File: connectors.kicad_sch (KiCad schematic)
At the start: 0 parts

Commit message: [#51627] Deserializer: add connections and passives
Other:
- company: (none) -> Antmicro Ltd
- title: (none) -> GMSL Deserializer
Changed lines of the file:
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@@
 (kicad_sch (version 20211123) (generator eeschema)
   (paper "A3")
+  (title_block
+    (title "GMSL Deserializer")
+    (date "2023-11-23")
+    (rev "1.0.0")
+    (company "Antmicro Ltd")
+    (comment 1 "www.antmicro.com")
+  )
 )

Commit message: [#51628] Connectors: add CSI mux and FFC connectors
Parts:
- added C? (x4): C_1u_0402, jetson-orin-baseboard-footprints:C_0402_1005Metric, symbol jetson-orin-baseboard:C_1u_0402
- added D? (x4): LED_G_0603_LTST-C190GKT, jetson-orin-baseboard-footprints:LED_0603_1608Metric_G, symbol jetson-orin-baseboard:LED_G_0603_LTST-C190GKT
- added J? (x2): Conn_FFC_68715014522_ONE-SIDE, jetson-orin-baseboard-footprints:WE_68715014522_ONE-SIDE, symbol jetson-orin-baseboard:Conn_FFC_68715014522_ONE-SIDE
- added R? (x6): R_4x0R_0201_array, jetson-orin-baseboard-footprints:R_Array_4x0201_Panasonic_EXB18V, symbol jetson-orin-baseboard:R_4x0R_0201_array
- added R? (x2): R_470R_0402, jetson-orin-baseboard-footprints:R_0402_1005Metric, symbol jetson-orin-baseboard:R_470R_0402
- added R? (x2): R_200R_0402, jetson-orin-baseboard-footprints:R_0402_1005Metric, symbol jetson-orin-baseboard:R_200R_0402
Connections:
- new net: D?.1, R?.1 (x4)
- new net: J?.42, R?.5 (R4.2) (x2)
- new net: J?.41, R?.6 (R3.2) (x2)
- new net: J?.40, R?.7 (R2.2) (x2)
- new net: J?.39, R?.8 (R1.2) (x2)
- new net CSI0_CLK_N: J?.10
- new net CSI0_CLK_P: J?.11
- new net CSI0_D0_N: J?.7, R?.3 (R3.1), R?.3 (R3.1)
- new net CSI0_D0_P: J?.8, R?.4 (R4.1), R?.4 (R4.1)
- new net CSI0_D1_N: R?.1 (R1.1), R?.1 (R1.1)
- new net CSI0_D1_P: J?.6, R?.2 (R2.1), R?.2 (R2.1)
- new net CSI1_0_D0_N: J?.3
- new net CSI1_0_D0_P: J?.4
- new net CSI1_0_D1_N: J?.1
- new net CSI1_0_D1_P: J?.2
- new net CSI1_1_D0_N: J?.7
- new net CSI1_1_D0_P: J?.8
- new net CSI1_1_D1_N: J?.5
- new net CSI1_1_D1_P: J?.6
- new net CSI1_CLK_N: J?.10
- new net CSI1_CLK_P: J?.11
- new net CSI2_CLK_N: J?.28
- new net CSI2_CLK_P: J?.29
- new net CSI2_D0_N: J?.25, R?.3 (R3.1), R?.3 (R3.1)
- new net CSI2_D0_P: J?.26, R?.4 (R4.1), R?.4 (R4.1)
- new net CSI2_D1_N: J?.23, R?.1 (R1.1), R?.1 (R1.1)
- new net CSI2_D1_P: J?.24, R?.2 (R2.1), R?.2 (R2.1)
- new net CSI3_0_D0_N: J?.21
- new net CSI3_0_D0_P: J?.22
- new net CSI3_0_D1_N: J?.19
- new net CSI3_0_D1_P: J?.20
- new net CSI3_1_D0_N: J?.25
- new net CSI3_1_D0_P: J?.26
- new net CSI3_1_D1_N: J?.23
- new net CSI3_1_D1_P: J?.24
- new net CSI3_CLK_N: J?.28
- new net CSI3_CLK_P: J?.29
- new net CSIA_3V3: C?.2, J?.47, J?.48, R?.2
- new net CSIA_5V: C?.2, J?.49, J?.50, R?.2
- new net CSIB_3V3: C?.2, J?.47, J?.48, R?.2
- new net CSIB_5V: C?.2, J?.49, J?.50, R?.2
- new net GND: C?.1, C?.1, C?.1, C?.1, D?.2, D?.2, D?.2, D?.2, J?.12, J?.12, J?.15, J?.15, J?.18, J?.18, J?.27, J?.27, J?.30, J?.30, J?.9, J?.9, J?.SH, J?.SH
- new net SCL_CAM0: R?.2 (R2.1)
- new net SCL_CAM1: R?.4 (R4.1)
- new net SCL_CAM2: R?.2 (R2.1)
- new net SCL_CAM3: R?.4 (R4.1)
- new net SDA_CAM0: R?.1 (R1.1)
- new net SDA_CAM1: R?.3 (R3.1)
- new net SDA_CAM2: R?.1 (R1.1)
- new net SDA_CAM3: R?.3 (R3.1)
- new net VSYNC_CAM0_3V3: J?.32
- new net VSYNC_CAM1_3V3: J?.34
- new net VSYNC_CAM2_3V3: J?.32
- new net VSYNC_CAM3_3V3: J?.34
- no-connect marks 0 -> 36
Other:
- note added: "CSI Mux"
- note added: "CSI connector J?"
- note added: "CSI0 x2"
- note added: "CSI0 x4"
- note added: "CSI1 x2"
- note added: "CSI2 x2"
- note added: "CSI2 x4"
- note added: "CSI3 x2"

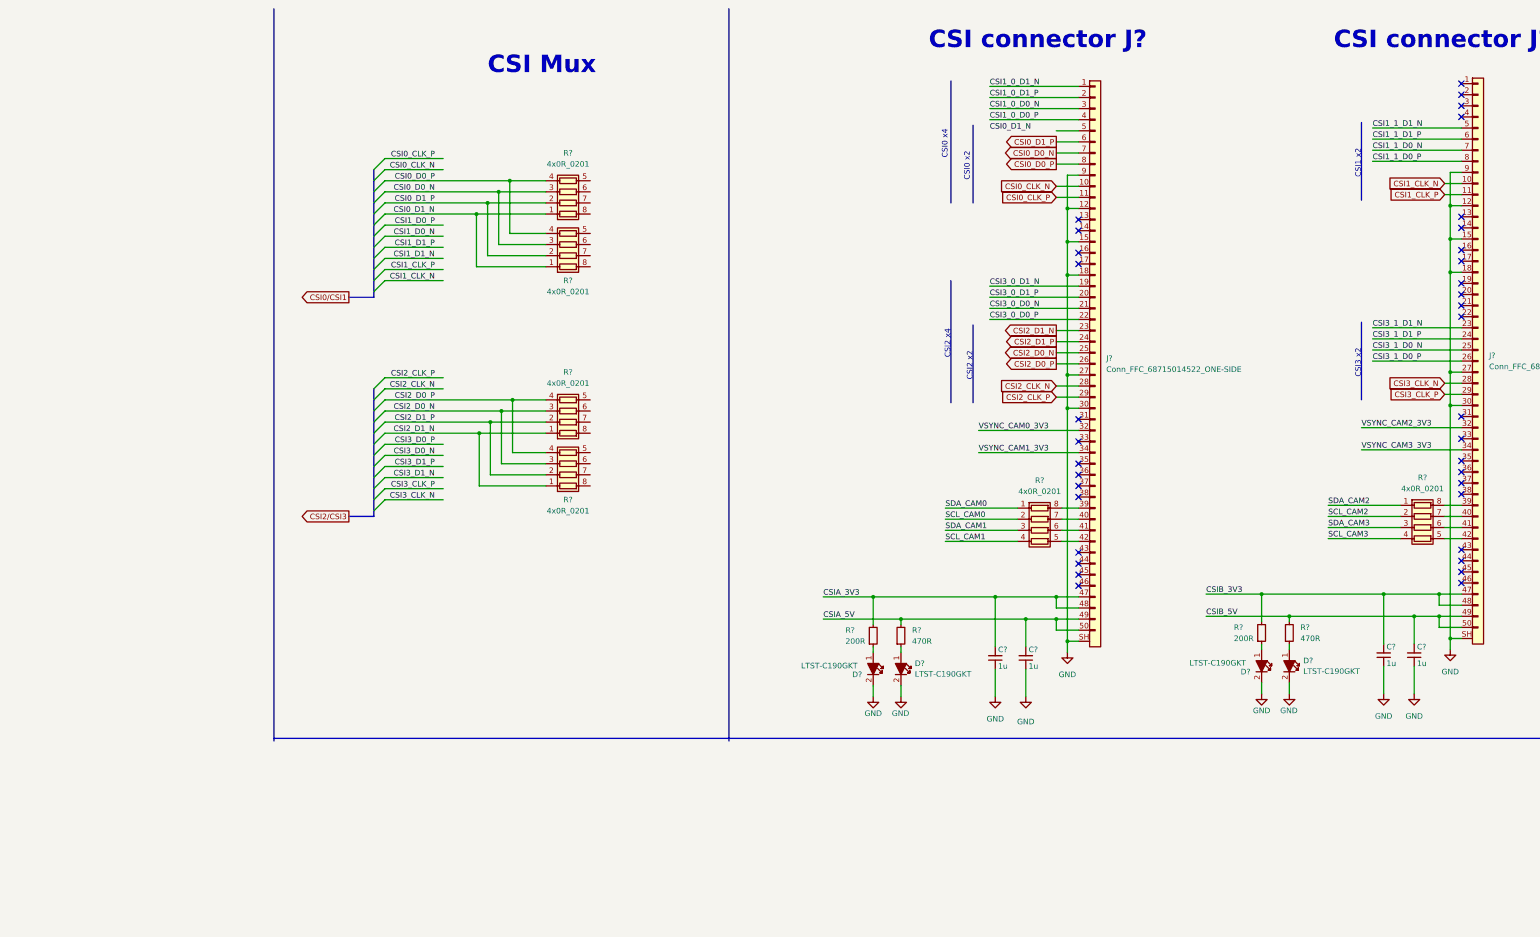
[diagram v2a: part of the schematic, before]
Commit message: [#51628] Connectors: add FAKRA connectors and CSI nets
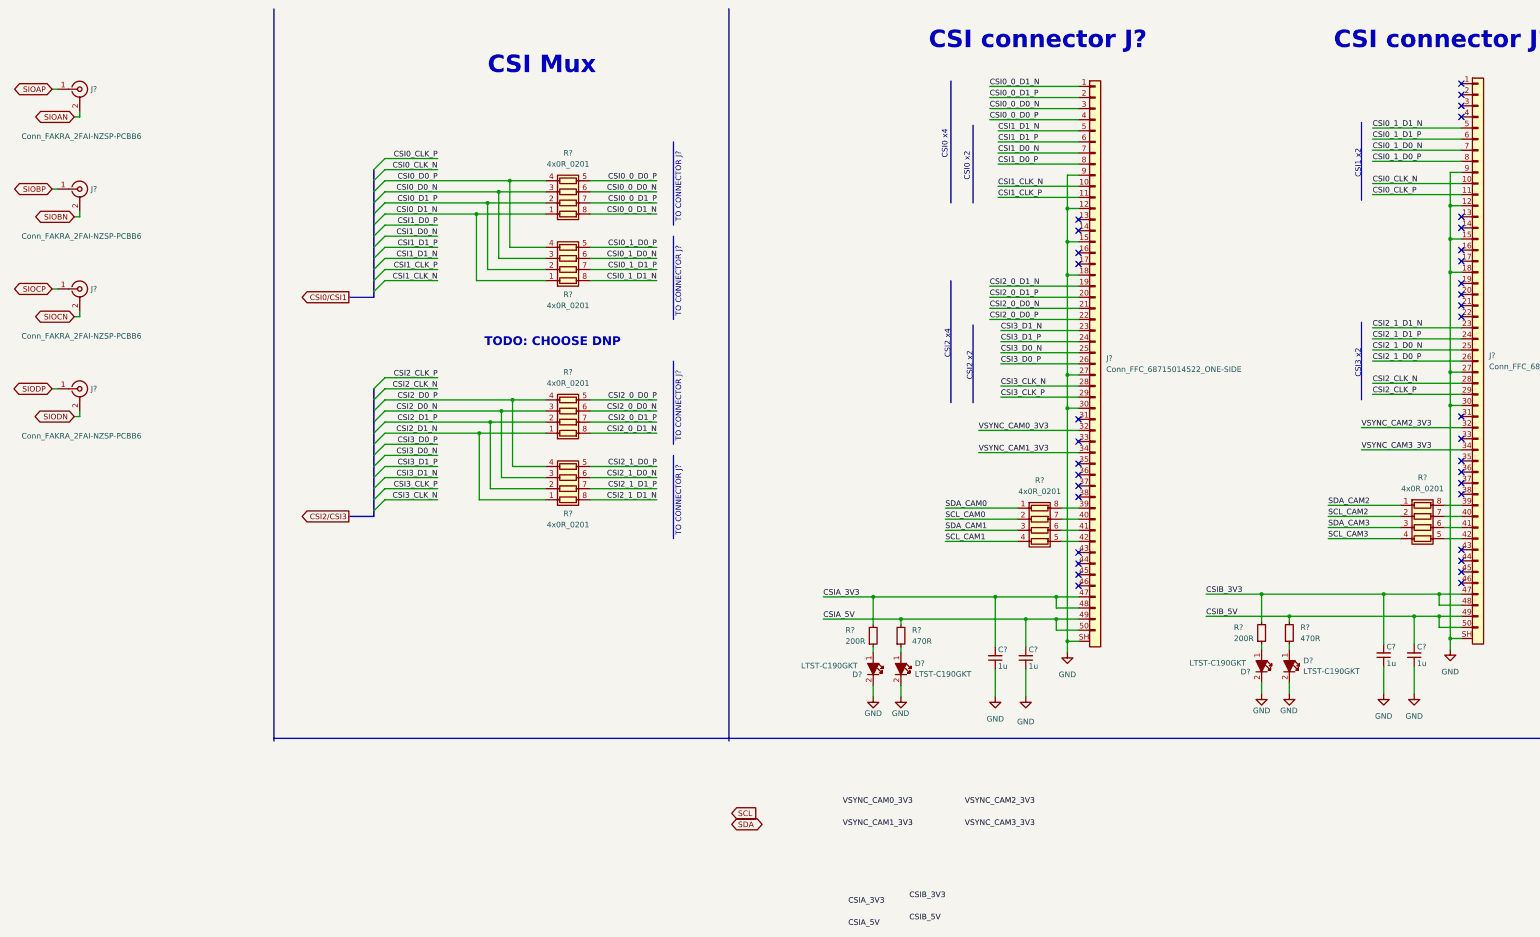
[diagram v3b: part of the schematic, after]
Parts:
- added J? (x4): Conn_FAKRA_2FAI-NZSP-PCBB6, antmicro-footprints:Conn_FAKRA_2FAI-NXSP-PCBB6, symbol antmicroCoaxialConnectorsRF:Conn_FAKRA_2FAI-NZSP-PCBB6
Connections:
- net CSI1_0_D0_N is gone; now on net CSI0_0_D0_N: J?.3
- net CSI1_0_D0_P is gone; now on net CSI0_0_D0_P: J?.4
- net CSI1_0_D1_N is gone; now on net CSI0_0_D1_N: J?.1
- net CSI1_0_D1_P is gone; now on net CSI0_0_D1_P: J?.2
- net CSI1_1_D0_N is gone; now on net CSI0_1_D0_N: J?.7
- net CSI1_1_D0_P is gone; now on net CSI0_1_D0_P: J?.8
- net CSI1_1_D1_N is gone; now on net CSI0_1_D1_N: J?.5
- net CSI1_1_D1_P is gone; now on net CSI0_1_D1_P: J?.6
- net CSI3_0_D0_N is gone; now on net CSI2_0_D0_N: J?.21
- net CSI3_0_D0_P is gone; now on net CSI2_0_D0_P: J?.22
- net CSI3_0_D1_N is gone; now on net CSI2_0_D1_N: J?.19
- net CSI3_0_D1_P is gone; now on net CSI2_0_D1_P: J?.20
- net CSI3_1_D0_N is gone; now on net CSI2_1_D0_N: J?.25
- net CSI3_1_D0_P is gone; now on net CSI2_1_D0_P: J?.26
- net CSI3_1_D1_N is gone; now on net CSI2_1_D1_N: J?.23
- net CSI3_1_D1_P is gone; now on net CSI2_1_D1_P: J?.24
- net CSI0_CLK_N: now also J?.10; no longer J?.10
- net CSI0_CLK_P: now also J?.11; no longer J?.11
- net CSI0_D0_N: no longer J?.7
- net CSI0_D0_P: no longer J?.8
- net CSI0_D1_P: no longer J?.6
- net CSI1_CLK_N: now also J?.10; no longer J?.10
- net CSI1_CLK_P: now also J?.11; no longer J?.11
- net CSI1_D0_N: now also J?.7
- net CSI1_D0_P: now also J?.8
- net CSI1_D1_N: now also J?.5
- net CSI1_D1_P: now also J?.6
- net CSI2_CLK_N: now also J?.28; no longer J?.28
- net CSI2_CLK_P: now also J?.29; no longer J?.29
- net CSI2_D0_N: no longer J?.25
- net CSI2_D0_P: no longer J?.26
- net CSI2_D1_N: no longer J?.23
- net CSI2_D1_P: no longer J?.24
- net CSI3_CLK_N: now also J?.28; no longer J?.28
- net CSI3_CLK_P: now also J?.29; no longer J?.29
- net CSI3_D0_N: now also J?.25
- net CSI3_D0_P: now also J?.26
- net CSI3_D1_N: now also J?.23
- net CSI3_D1_P: now also J?.24
- net CSI0_0_D0_P: now reaches R?.5 (R4.2)
- net CSI0_0_D0_N: now reaches R?.6 (R3.2)
- net CSI0_0_D1_P: now reaches R?.7 (R2.2)
- net CSI0_0_D1_N: now reaches R?.8 (R1.2)
- net CSI0_1_D0_P: now reaches R?.5 (R4.2)
- net CSI0_1_D0_N: now reaches R?.6 (R3.2)
- net CSI0_1_D1_P: now reaches R?.7 (R2.2)
- net CSI0_1_D1_N: now reaches R?.8 (R1.2)
- net CSI2_1_D0_P: now reaches R?.5 (R4.2)
- net CSI2_1_D0_N: now reaches R?.6 (R3.2)
- net CSI2_1_D1_P: now reaches R?.7 (R2.2)
- net CSI2_1_D1_N: now reaches R?.8 (R1.2)
- net CSI2_0_D0_P: now reaches R?.5 (R4.2)
- net CSI2_0_D0_N: now reaches R?.6 (R3.2)
- net CSI2_0_D1_P: now reaches R?.7 (R2.2)
- net CSI2_0_D1_N: now reaches R?.8 (R1.2)
- new net SIOAN: J?.2, J?.3, J?.4, J?.5
- new net SIOAP: J?.1
- new net SIOBN: J?.2, J?.3, J?.4, J?.5
- new net SIOBP: J?.1
- new net SIOCN: J?.2, J?.3, J?.4, J?.5
- new net SIOCP: J?.1
- new net SIODN: J?.2, J?.3, J?.4, J?.5
- new net SIODP: J?.1
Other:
- note added: "TO CONNECTOR J?"
- note added: "TODO: CHOOSE DNP"
- moved on the sheet: R?

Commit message: [#51628] Connectors: change FAKRA connectors and add Multi-function pins
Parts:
- removed R? (x2): R_4x0R_0201_array, jetson-orin-baseboard-footprints:R_Array_4x0201_Panasonic_EXB18V, symbol jetson-orin-baseboard:R_4x0R_0201_array
- added R? (x8): R_0R_0402, antmicro-footprints:R_0402_1005Metric, symbol antmicroResistors0402:R_0R_0402
- added TP? (x4): TP_0.75mm_SMD, antmicro-footprints:TP_SMD_0.75mm, symbol antmicroTestPoints:TP_0.75mm_SMD
- J? (x4): footprint antmicro-footprints:Conn_FAKRA_2FAI-NXSP-PCBB6 -> antmicro-footprints:Conn_FAKRA_59S2AQ-40MT5-Z_1; symbol antmicroCoaxialConnectorsRF:Conn_FAKRA_2FAI-NZSP-PCBB6 -> antmicroCoaxialConnectorsRF:Conn_FAKRA_59S2AQ-40MT5-Z_1; MPN 2FAI-NZSP-PCBB6 -> 59S2AQ-40MT5-Z_1; Manufacturer Amphenol -> Rosenberger
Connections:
- net SCL: now also R?.2, R?.2, R?.2, R?.2
- net SDA: now also R?.2, R?.2, R?.2, R?.2
- net at J?.42: now also R?.1 (x2)
- net at J?.41: now also R?.1 (x2)
- net at J?.40: now also R?.1 (x2)
- net at J?.39: now also R?.1 (x2)
- net VSYNC_CAM0_3V3 renamed MFP1
- net VSYNC_CAM1_3V3 renamed MFP3
- net VSYNC_CAM2_3V3 renamed MFP7
- net VSYNC_CAM3_3V3 renamed MFP8
- new net MFP0: TP?.1
- new net MFP2: TP?.1
- new net MFP4: TP?.1
- new net MFP5: TP?.1
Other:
- note added: "Fakra connectors"
- note added: "Multi-function pins"
- moved on the sheet: J?

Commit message: [#51632] Power: add current limit, buck conv Connectors: add buffer gates, remove one FFC conn
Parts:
- removed C? (x4): C_1u_0402, jetson-orin-baseboard-footprints:C_0402_1005Metric, symbol jetson-orin-baseboard:C_1u_0402
- removed D? (x4): LED_G_0603_LTST-C190GKT, jetson-orin-baseboard-footprints:LED_0603_1608Metric_G, symbol jetson-orin-baseboard:LED_G_0603_LTST-C190GKT
- removed J? (x2): Conn_FFC_68715014522_ONE-SIDE, jetson-orin-baseboard-footprints:WE_68715014522_ONE-SIDE, symbol jetson-orin-baseboard:Conn_FFC_68715014522_ONE-SIDE
- removed R? (x4): R_0R_0402, antmicro-footprints:R_0402_1005Metric, symbol antmicroResistors0402:R_0R_0402
- removed R? (x4): R_4x0R_0201_array, jetson-orin-baseboard-footprints:R_Array_4x0201_Panasonic_EXB18V, symbol jetson-orin-baseboard:R_4x0R_0201_array
- removed R? (x2): R_470R_0402, jetson-orin-baseboard-footprints:R_0402_1005Metric, symbol jetson-orin-baseboard:R_470R_0402
- removed R? (x2): R_200R_0402, jetson-orin-baseboard-footprints:R_0402_1005Metric, symbol jetson-orin-baseboard:R_200R_0402
- removed TP? (x4): TP_0.75mm_SMD, antmicro-footprints:TP_SMD_0.75mm, symbol antmicroTestPoints:TP_0.75mm_SMD
- added C? (x2): C_100n_0402, antmicro-footprints:C_0402_1005Metric, symbol antmicroCapacitors0402:C_100n_0402
- added C?: C_1u_0402, antmicro-footprints:C_0402_1005Metric, symbol antmicroCapacitors0402:C_1u_0402
- added D?: LED_G_0603_LTST-C190GKT, antmicro-footprints:LED_0603_1608Metric_G, symbol antmicroLEDIndicationDiscrete:LED_G_0603_LTST-C190GKT
- added F?: F_3A_1206, antmicro-footprints:F_1206_3216Metric, symbol antmicroFuses:F_3A_1206
- added J?: BarrelJack_PJ-063BH, antmicro-footprints:BarrelJack_PJ-063BH, symbol antmicroBarrelPowerConnectors:BarrelJack_PJ-063BH
- added J?: Conn_FFC_WE_68715014522, antmicro-footprints:Conn_FFC_WE_68715014x22, symbol antmicroFCCConnectors:Conn_FFC_WE_68715014522
- added R? (x6): R_0R_0402, antmicro-footprints:R_0402_1005Metric, symbol antmicroResistors0402:R_0R_0402
- added R? (x2): R_10k_0402, antmicro-footprints:R_0402_1005Metric, symbol antmicroResistors0402:R_10k_0402
- added R?: R_200R_0402, antmicro-footprints:R_0402_1005Metric, symbol antmicroResistors0402:R_200R_0402
- added R?: R_470R_0402, antmicro-footprints:R_0402_1005Metric, symbol antmicroResistors0402:R_470R_0402
- added TP? (x4): TP_0.75mm_SMD, antmicro-footprints:TP_SMD_0.75mm, symbol antmicroTestPoints:TP_0.75mm_SMD
- added U? (x2): SN74LV1T125DBVR, antmicro-footprints:SOT-23-5, symbol antmicroLogicBuffersDriversReceiversTransceivers:SN74LV1T125DBVR
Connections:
- net SIOAN is gone; now on net GND: J?.2, J?.3, J?.4, J?.5
- net SIOBN is gone; now on net GND: J?.2, J?.3, J?.4, J?.5
- net SIOCN is gone; now on net GND: J?.2, J?.3, J?.4, J?.5
- net SIODN is gone; now on net GND: J?.2, J?.3, J?.4, J?.5
- net CSI0_D0_N: now also J?.3
- net CSI0_D0_P: now also J?.4
- net CSI0_D1_N: now also J?.1
- net CSI0_D1_P: now also J?.2
- net CSI1_CLK_N: now also J?.10
- net CSI1_CLK_P: now also J?.11
- net CSI1_D0_N: now also J?.7
- net CSI1_D0_P: now also J?.8
- net CSI1_D1_N: now also J?.5
- net CSI1_D1_P: now also J?.6
- net CSI2_D0_N: now also J?.21
- net CSI2_D0_P: now also J?.22
- net CSI2_D1_N: now also J?.19
- net CSI2_D1_P: now also J?.20
- net CSI3_CLK_N: now also J?.28
- net CSI3_CLK_P: now also J?.29
- net CSI3_D0_N: now also J?.25
- net CSI3_D0_P: now also J?.26
- net CSI3_D1_N: now also J?.23
- net CSI3_D1_P: now also J?.24
- net GND: now also C?.1, C?.1, C?.1, D?.2, J?.12, J?.15, J?.18, J?.2, J?.27, J?.30, J?.9, J?.MP1 (MP), J?.MP2 (MP), J?.SH, R?.1, R?.1, U?.3 (GND), U?.3 (GND)
- net MFP0: now also R?.1
- net MFP1: now also R?.1
- net MFP2: now also R?.1
- net MFP3: now also R?.1
- net MFP4: now also TP?.1
- net MFP5: now also TP?.1
- net MFP7: now also TP?.1
- net MFP8: now also TP?.1
- net at R?.1: now also J?.39
- net at R?.1: now also J?.41
- net at R?.1: now also J?.40
- net at R?.1: now also J?.42
- net SIOAP renamed PoCA
- net SIOBP renamed PoCB
- net SIOCP renamed PoCC
- net SIODP renamed PoCD
- new net: F?.1, J?.1
- new net: R?.2, R?.2, U?.4 (Y) (x2)
- new net: R?.2, U?.1 (~{OE}) (x2)
- new net: D?.1, R?.1
- new net: J?.32, R?.1
- new net: J?.34, R?.1
- new net +1V8: C?.2, C?.2, U?.5 (VCC), U?.5 (VCC)
- new net DC_IN: F?.2
- new net FFC_5V: C?.2, J?.49, J?.50, R?.2
- new net VSYNC_CAM0: R?.2, R?.2, U?.2 (A)
- new net VSYNC_CAM1: R?.1, R?.2, U?.2 (A)
- no-connect marks 36 -> 16
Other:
- note added: "Buffer gates"
- note added: "CSI connector"
- note added: "Power connector"
- note removed: "CSI Mux"
- note removed: "CSI connector J?"
- note removed: "CSI1 x2"
- note removed: "CSI3 x2"
- note removed: "TO CONNECTOR J?"
- note removed: "TODO: CHOOSE DNP"
- moved on the sheet: J?, R?

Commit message: Schematics done
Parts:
- removed J?: BarrelJack_PJ-063BH, antmicro-footprints:BarrelJack_PJ-063BH, symbol antmicroBarrelPowerConnectors:BarrelJack_PJ-063BH
- added C1: C_10u_25V_0603, antmicro-footprints:C_0603_1608Metric, symbol antmicroCapacitors0603:C_10u_25V_0603
- added C2: C_100n_0402, antmicro-footprints:C_0402_1005Metric, symbol antmicroCapacitors0402:C_100n_0402
- added D1: DF2S30FS_SOD, antmicro-footprints:SOD-923, symbol antmicroTVSDiodes:DF2S30FS_SOD
- added J1: Molex_Nano-Fit_1x2_SMD_1054301202, antmicro-footprints:Conn_Molex_Nano-Fit_1x2_SMD_1054301202, symbol antmicroWire2BoardConnectors:Molex_Nano-Fit_1x2_SMD_1054301202
- gave numbers to parts that had none: 30
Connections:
- net GND: now also C1.1, C2.1, D1.2, J1.2, J1.MP
- net at F1.1: now also C1.2, C2.2, D1.1, J1.1
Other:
- moved on the sheet: F1

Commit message: Schematics: Fix buses, change labels to hierarchical
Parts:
- J2, J3, J4, J5: value Conn_FAKRA_2FAI-NZSP-PCBB6 -> Conn_FAKRA_59S2AQ-40MT5-Z_1
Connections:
- net CSI0_D0_N renamed CSI0.D2_N
- net CSI0_D0_P renamed CSI0.D2_P
- net CSI0_D1_N renamed CSI0.D3_N
- net CSI0_D1_P renamed CSI0.D3_P
- net CSI1_CLK_N renamed CSI0.CLK_N
- net CSI1_CLK_P renamed CSI0.CLK_P
- net CSI1_D0_N renamed CSI0.D0_N
- net CSI1_D0_P renamed CSI0.D0_P
- net CSI1_D1_N renamed CSI0.D1_N
- net CSI1_D1_P renamed CSI0.D1_P
- net CSI2_D0_N renamed CSI1.D2_N
- net CSI2_D0_P renamed CSI1.D2_P
- net CSI2_D1_N renamed CSI1.D3_N
- net CSI2_D1_P renamed CSI1.D3_P
- net CSI3_CLK_N renamed CSI1.CLK_N
- net CSI3_CLK_P renamed CSI1.CLK_P
- net CSI3_D0_N renamed CSI1.D0_N
- net CSI3_D0_P renamed CSI1.D0_P
- net CSI3_D1_N renamed CSI1.D1_N
- net CSI3_D1_P renamed CSI1.D1_P
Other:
- moved on the sheet: C3, C4, C5, D2, J6, R1, R10, R11, R12, R13, R14, R2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
